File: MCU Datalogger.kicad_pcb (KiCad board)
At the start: 2 copper layers, 29 parts, among them J1 Conn_01x04_Pin, J2 Conn_01x04_Pin, J3 Conn_01x09_Pin, J4 Conn_02x03_Odd_Even, U1 24LC1025, U2 24LC1025, U3 DS1337S_, U4 ATMEGA328P-AU, Y1 32.768KHz, Y2 16MHz

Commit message: pcb layout setup
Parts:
- moved U3 19.5 mm to (70.5, 81.9)
- moved U4 18.9 mm to (37.5, 65.8)
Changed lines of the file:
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@@
 	(paper "A4")
 	(layers
-		(0 "F.Cu" signal)
-		(2 "B.Cu" signal)
+		(0 "F.Cu" mixed)
+		(2 "B.Cu" mixed)
 		(9 "F.Adhes" user "F.Adhesive")
 		(11 "B.Adhes" user "B.Adhesive")
@@
 	)
 	(setup
+		(stackup
+			(layer "F.SilkS"
+				(type "Top Silk Screen")
+			)
+			(layer "F.Paste"
+				(type "Top Solder Paste")
+			)
+			(layer "F.Mask"
+				(type "Top Solder Mask")
+				(thickness 0.01)
+			)
+			(layer "F.Cu"
+				(type "copper")
+				(thickness 0.035)
+			)
+			(layer "dielectric 1"
+				(type "core")
+				(thickness 1.51)
+				(material "FR4")
+				(epsilon_r 4.5)
+				(loss_tangent 0.02)
+			)
+			(layer "B.Cu"
+				(type "copper")
+				(thickness 0.035)
+			)
+			(layer "B.Mask"
+				(type "Bottom Solder Mask")
+				(thickness 0.01)
+			)
+			(layer "B.Paste"
+				(type "Bottom Solder Paste")
+			)
+			(layer "B.SilkS"
+				(type "Bottom Silk Screen")
+			)
+			(copper_finish "None")
+			(dielectric_constraints no)
+		)
 		(pad_to_mask_clearance 0)
 		(allow_soldermask_bridges_in_footprints no)
@@
 	(footprint "DS1337S_:SOIC127P600X175-8N"
 		(layer "F.Cu")
-		(at 70.108 101.46)
+		(at 70.547 81.915)
 		(property "Reference" "U3"
 			(at -0.795 -3.332 0)
@@
 	(footprint "ATMEGA328P-AU:QFP80P900X900X120-32N"
 		(layer "F.Cu")
-		(at 56.028 62.084)
+		(at 37.514 65.786)
 		(property "Reference" "U4"
 			(at -2.795 -6.79 0)

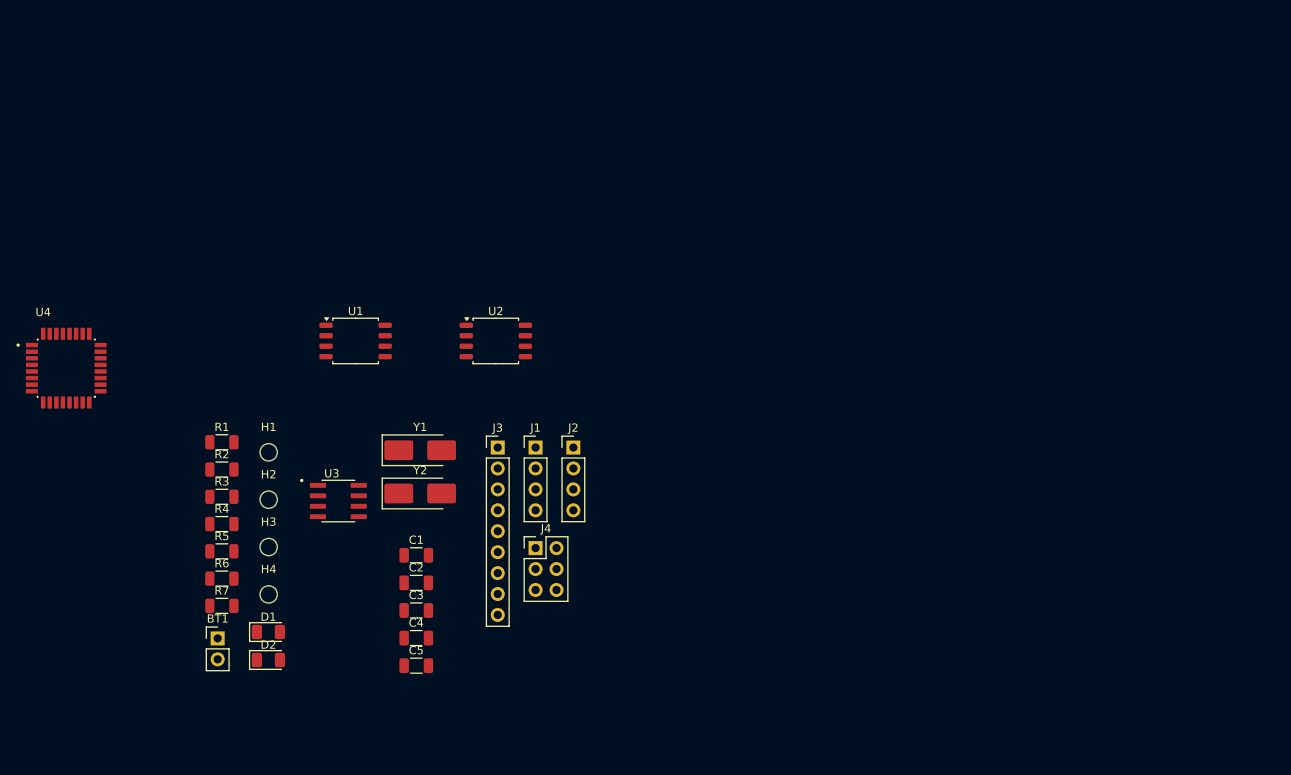
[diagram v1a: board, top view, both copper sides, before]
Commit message: complete layout of components
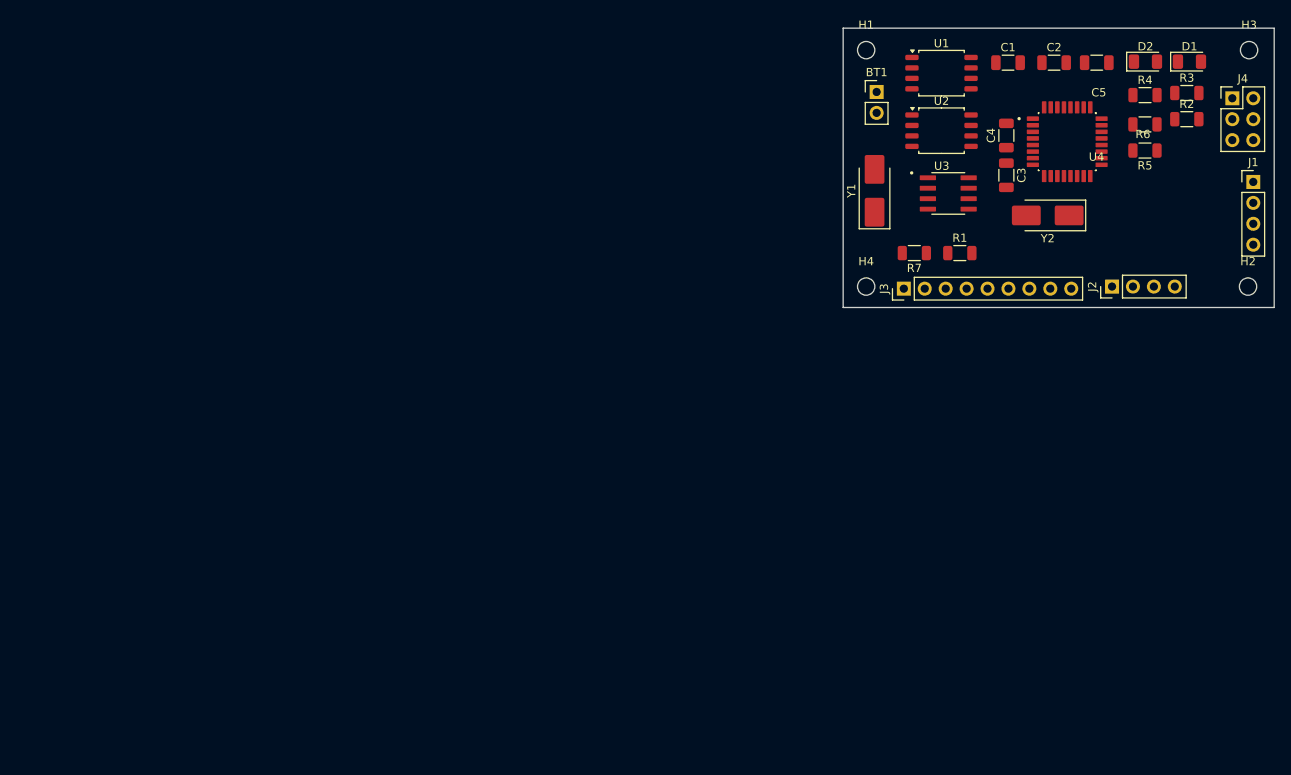
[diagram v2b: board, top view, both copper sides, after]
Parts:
- moved H3 133.4 mm to (181.1, 27.2)
- moved D1 131.5 mm to (173.9, 28.6)
- moved D2 128.9 mm to (168.5, 28.6)
- moved R3 127.0 mm to (173.5, 32.4)
- moved R6 124.9 mm to (168.5, 36.2), turned to 180 degrees
- moved R2 124.6 mm to (173.5, 35.6)
- moved U4 124.6 mm to (159.0, 38.3)
- moved R4 123.6 mm to (168.5, 32.6)
- moved R5 122.2 mm to (168.5, 39.4), turned to 180 degrees
- moved H2 121.7 mm to (181.0, 55.9)
- moved C5 110.4 mm to (162.6, 28.7), turned to 180 degrees
- moved BT1 103.9 mm to (135.9, 32.3)
- moved J4 100.7 mm to (179.1, 33.0)
- moved C2 99.9 mm to (157.4, 28.7)
- moved R7 94.3 mm to (140.5, 51.8), turned to 180 degrees
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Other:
- board outline added: 52.3 x 33.9 mm

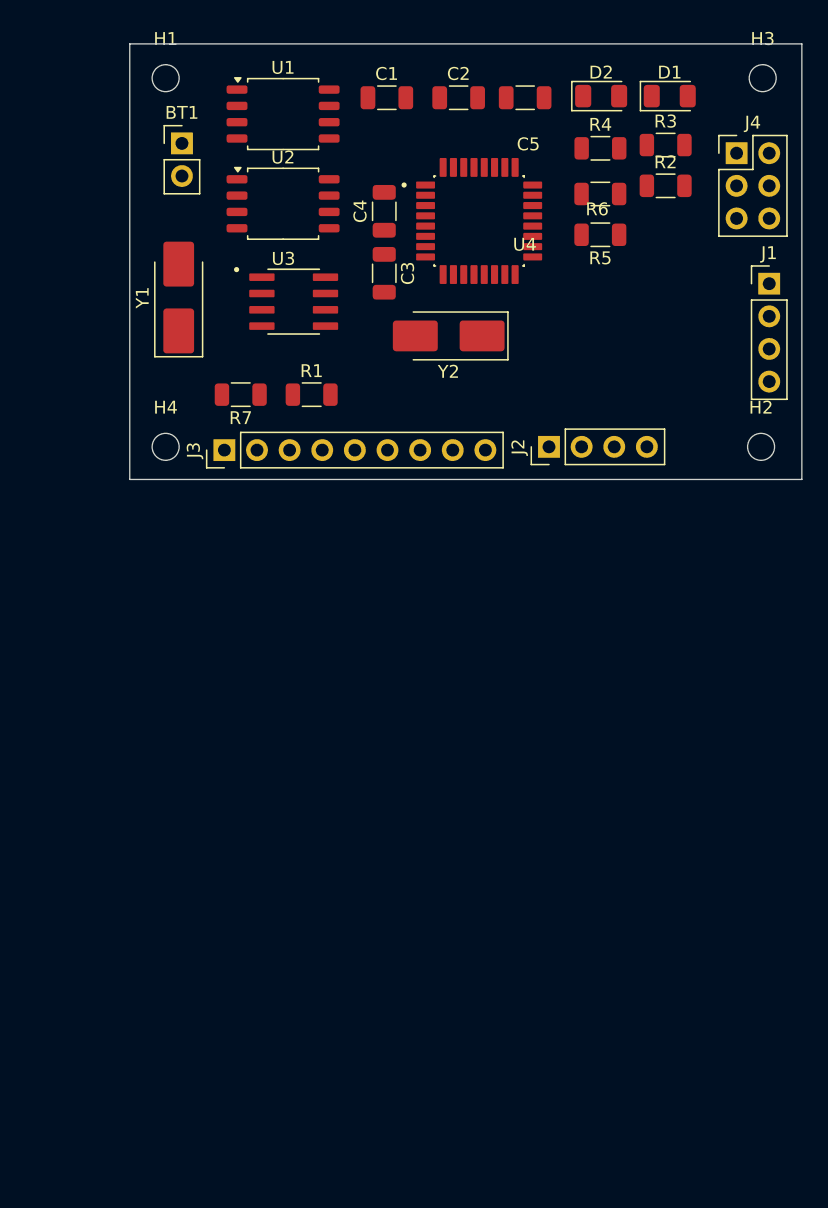
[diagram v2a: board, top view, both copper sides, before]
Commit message: drew proper shape of board & routed circuits partially
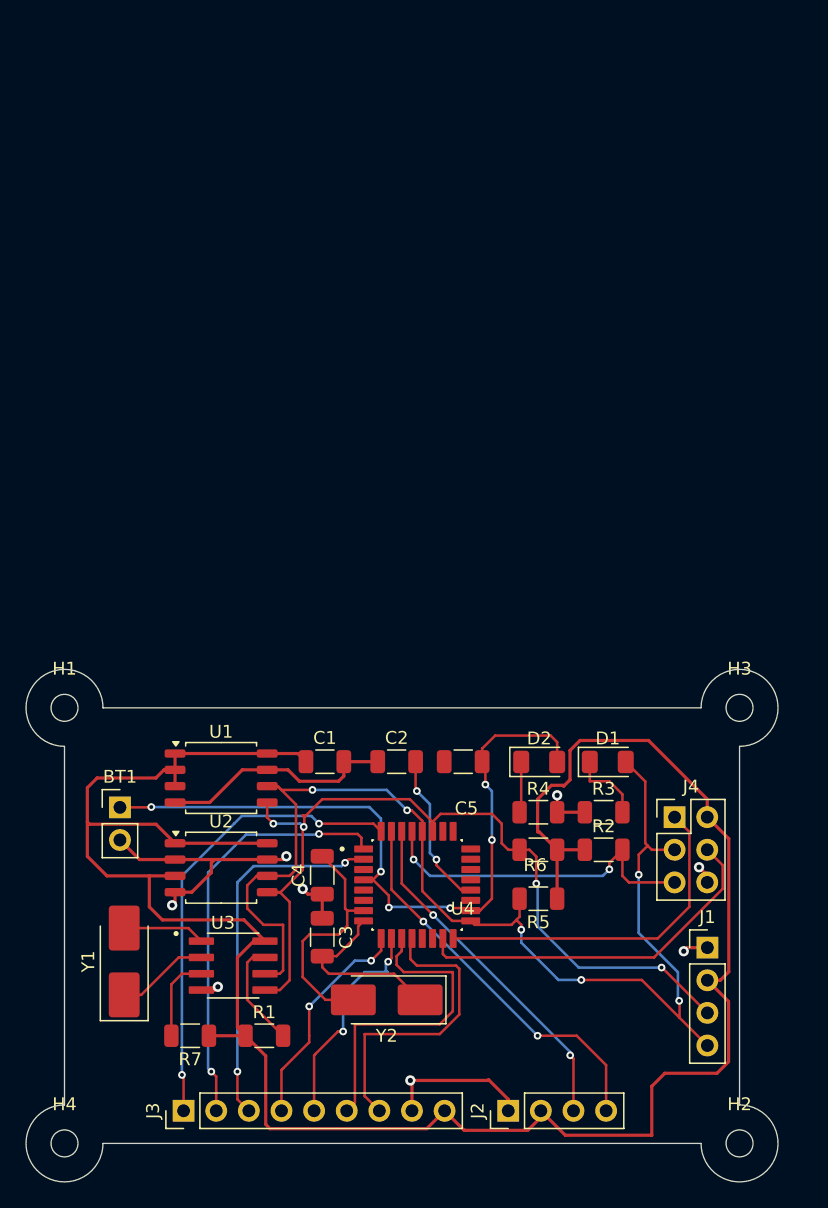
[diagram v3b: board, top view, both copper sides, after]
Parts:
- moved H4 54.8 mm to (126.7, 110.1)
- moved H2 54.3 mm to (179.3, 110.1)
- moved R3 52.2 mm to (168.7, 84.3)
- moved D1 52.1 mm to (169.0, 80.4)
- moved D2 52.1 mm to (163.7, 80.4)
- moved R4 51.9 mm to (163.6, 84.3)
- moved R5 51.9 mm to (163.6, 91.1)
- moved C1 51.9 mm to (147.0, 80.4)
- moved C2 51.9 mm to (152.6, 80.4)
- moved C3 51.9 mm to (146.8, 94.1)
- moved C5 51.9 mm to (157.8, 80.4)
- moved U4 51.9 mm to (154.2, 90.0)
- moved Y2 51.9 mm to (151.8, 98.9)
- moved BT1 51.9 mm to (131.1, 83.9)
- moved C4 51.9 mm to (146.8, 89.2)
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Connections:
- net SCK renamed /SCK
- net SDA renamed /SDA
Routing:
- net /Vcc: track 0.00 -> 175.4 mm
- net /SCK: track 0.00 -> 94.8 mm, vias 0 -> 6
- net /SDA: track 0.00 -> 66.8 mm, vias 0 -> 4
- net GND: track 0.00 -> 61.6 mm, vias 0 -> 8
- net Net-(BT1-+): track 0.00 -> 58.9 mm, vias 0 -> 6
- net /D2: track 0.00 -> 36.3 mm, vias 0 -> 2
- net /D3: track 0.00 -> 33.1 mm, vias 0 -> 2
- net /TX: track 0.00 -> 30.5 mm, vias 0 -> 2
- net /MOSI: track 0.00 -> 28.9 mm
- net /D4: track 0.00 -> 28.7 mm, vias 0 -> 2
- net /RX: track 0.00 -> 27.3 mm, vias 0 -> 2
- net /MISO: track 0.00 -> 26.9 mm
- net /RESET: track 0.00 -> 26.5 mm, vias 0 -> 2
- net /D7: track 0.00 -> 24.9 mm
- net /D8: track 0.00 -> 23.8 mm
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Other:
- board size 52.3 x 33.9 mm -> 58.5 x 39.9 mm
